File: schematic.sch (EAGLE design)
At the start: 14 parts, among them IC1 REG1117

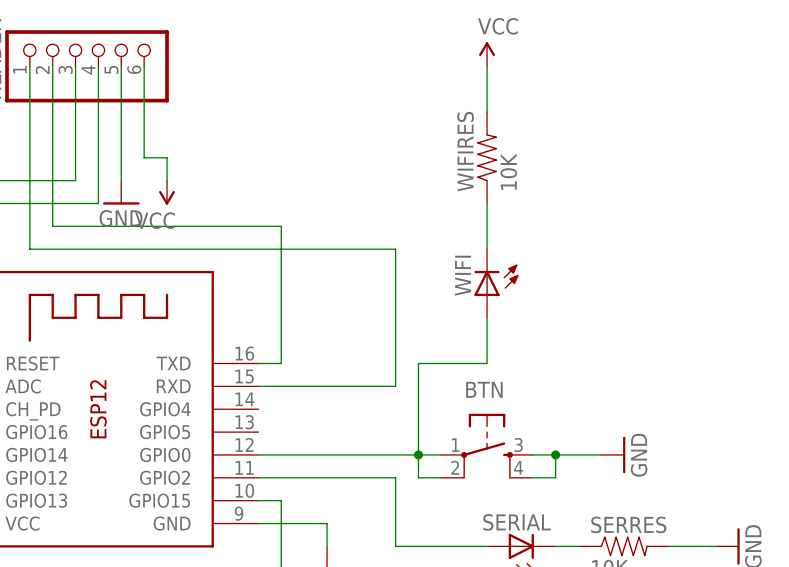
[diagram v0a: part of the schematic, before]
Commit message: changed led rotation
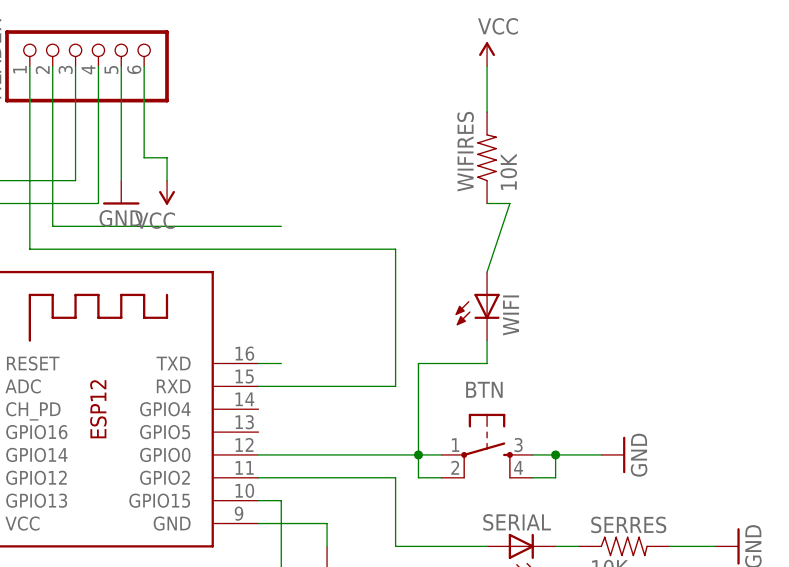
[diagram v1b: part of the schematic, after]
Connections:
- new net N$13: WIFI.A, WIFIRES.1
- net N$2: no longer X1.TXD
- net N$5: now also WIFI.C; no longer WIFI.A
- net N$7: now also X1.TXD; no longer WIFI.C, WIFIRES.1
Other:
- moved on the sheet: WIFI
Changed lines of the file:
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@@
 <instance part="SERRES" gate="G$1" x="121.92" y="27.94"/>
 <instance part="WIFIRES" gate="G$1" x="106.68" y="71.12" rot="R90"/>
-<instance part="WIFI" gate="G$1" x="106.68" y="55.88" rot="R180"/>
+<instance part="WIFI" gate="G$1" x="106.68" y="55.88"/>
 <instance part="GND4" gate="1" x="134.62" y="27.94" rot="R90"/>
 <instance part="SUPPLY3" gate="G$1" x="25.4" y="43.18" rot="R90"/>
@@
 <wire x1="58.42" y1="81.28" x2="58.42" y2="63.5" width="0.1524" layer="91"/>
 <wire x1="58.42" y1="63.5" x2="83.82" y2="63.5" width="0.1524" layer="91"/>
-<wire x1="83.82" y1="63.5" x2="83.82" y2="48.26" width="0.1524" layer="91"/>
-<pinref part="X1" gate="G$1" pin="TXD"/>
-<wire x1="83.82" y1="48.26" x2="81.28" y2="48.26" width="0.1524" layer="91"/>
 </segment>
 </net>
@@
 <wire x1="99.06" y1="35.56" x2="99.06" y2="38.1" width="0.1524" layer="91"/>
 <junction x="99.06" y="38.1"/>
-<pinref part="WIFI" gate="G$1" pin="A"/>
-<wire x1="106.68" y1="53.34" x2="106.68" y2="48.26" width="0.1524" layer="91"/>
 <wire x1="106.68" y1="48.26" x2="99.06" y2="48.26" width="0.1524" layer="91"/>
 <wire x1="99.06" y1="48.26" x2="99.06" y2="38.1" width="0.1524" layer="91"/>
+<pinref part="WIFI" gate="G$1" pin="C"/>
+<wire x1="106.68" y1="50.8" x2="106.68" y2="48.26" width="0.1524" layer="91"/>
 </segment>
 </net>
@@
 <pinref part="SERRES" gate="G$1" pin="1"/>
 <wire x1="114.3" y1="27.94" x2="116.84" y2="27.94" width="0.1524" layer="91"/>
-</segment>
-</net>
-<net name="N$7" class="0">
-<segment>
-<pinref part="WIFI" gate="G$1" pin="C"/>
-<pinref part="WIFIRES" gate="G$1" pin="1"/>
-<wire x1="106.68" y1="60.96" x2="106.68" y2="66.04" width="0.1524" layer="91"/>
 </segment>
 </net>
@@
 </segment>
 </net>
+<net name="N$7" class="0">
+<segment>
+<pinref part="X1" gate="G$1" pin="TXD"/>
+<wire x1="83.82" y1="48.26" x2="81.28" y2="48.26" width="0.1524" layer="91"/>
+</segment>
+</net>
+<net name="N$13" class="0">
+<segment>
+<pinref part="WIFI" gate="G$1" pin="A"/>
+<pinref part="WIFIRES" gate="G$1" pin="1"/>
+<wire x1="106.68" y1="66.04" x2="109.22" y2="66.04" width="0.1524" layer="91"/>
+<wire x1="109.22" y1="66.04" x2="106.68" y2="58.42" width="0.1524" layer="91"/>
+</segment>
+</net>
